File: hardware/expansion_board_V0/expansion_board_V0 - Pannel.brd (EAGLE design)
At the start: 212 x 132 mm, 499 parts, among them CON1 ELEC, CON10 M5, CON11 M2, CON12 M4, CON13 M1, CON14 ESC0, CON15 CON10_2_2.54, CON16 CON10_2_2.54, CON17 ESC1, CON18 UART0, CON19 QEI1, CON2 SERVO, CON20 AN0, CON21 S0, CON22 IO0, CON23 AN1, CON24 S1, CON25 IO1, CON26 UART1, CON27 QEI0, CON28 AN2, CON29 S2, CON3 LIPO_MOT, CON30 IO2, CON31 TELEM, CON32 QEI3, CON33 AN3, CON34 S3, CON35 IO3, CON36 BALISE, CON37 AN4, CON38 S4, CON39 IO4, CON4 LIPO_MOT, CON40 SPI0, CON41 QEI2, CON42 AN5, CON43 S5, CON44 IO5, CON45 SPI1, CON46 AN6, CON47 S6, CON48 IO6, CON49 I2C0, CON5 LIPO_MOT, CON50 AN7, CON51 S7, CON52 IO7, CON53 I2C1, CON54 USB2, CON55 USB3, CON56 USBfpga, CON57 FPGA_GPIO0, CON58 FPGA_GPIO1, CON59 FPGA_LTC, CON6 LIPO_MOT, CON60 USB3, CON61 CON5_2.54S, CON62 CON5_2.54S, CON63 CON5_2.54S, CON64 CON5_2.54S, CON7 FPGApower, CON8 M0, CON9 M3, IC1 ADS1258, IC2 ADS1278, IC3 REF5030I, IC4 REF5025I, J1 NC, J10 0, J11 0, J12 0, J13 0, J14 0, J15 0, J16 0, J17 0, J18 0, J19 0, J2 nc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

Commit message: -
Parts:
- added C200, C201, C202, C203, C204, C205, C206, C207, C208, C209, C210, C211: 2u, iocene:CAPC1608X95N
- added CON65, CON66, CON67, CON68, CON69, CON70, CON71, CON72, CON73, CON74, CON75, CON76: CON5_2.54S, iocene:CON254P1270X400-5S
- added R111, R112, R113, R114, R115, R116, R117, R118, R119, R120, R121, R122: 10k, iocene:RESC1005X40N
- added U41, U47, U53: VL53L0X, iocene:VL53L0X
- added U42, U44, U48, U50, U54, U56: TCA6408A, iocene:QFN50P300X300X80-17N
- added U43, U45, U49, U51, U55, U57: LP5900SD-2.8, iocene:SON65P250X220X80-7N
- added U46, U52, U58: VL6180X, iocene:VL6180X
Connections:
- new net GND1: C200.P$2, C201.P$2, C202.P$2, C203.P$2, CON65.1, CON66.1, CON67.1, CON68.1, R111.2, R112.2, R113.2, R114.2, U41.P$12, U41.P$2, U41.P$3, U41.P$4, U41.P$6, U42.GND, U42.P$16, U42.P$6, U43.2, U43.3, U43.5, U43.GND, U44.GND, U44.P$16, U44.P$6, U45.2, U45.3, U45.5, U45.GND, U46.P$11, U46.P$12, U46.P$2, U46.P$3, U46.P$7, U46.P$9
- new net GND2: C204.P$2, C205.P$2, C206.P$2, C207.P$2, CON69.1, CON70.1, CON71.1, CON72.1, R115.2, R116.2, R117.2, R118.2, U47.P$12, U47.P$2, U47.P$3, U47.P$4, U47.P$6, U48.GND, U48.P$16, U48.P$6, U49.2, U49.3, U49.5, U49.GND, U50.GND, U50.P$16, U50.P$6, U51.2, U51.3, U51.5, U51.GND, U52.P$11, U52.P$12, U52.P$2, U52.P$3, U52.P$7, U52.P$9
- new net GND3: C208.P$2, C209.P$2, C210.P$2, C211.P$2, CON73.1, CON74.1, CON75.1, CON76.1, R119.2, R120.2, R121.2, R122.2, U53.P$12, U53.P$2, U53.P$3, U53.P$4, U53.P$6, U54.GND, U54.P$16, U54.P$6, U55.2, U55.3, U55.5, U55.GND, U56.GND, U56.P$16, U56.P$6, U57.2, U57.3, U57.5, U57.GND, U58.P$11, U58.P$12, U58.P$2, U58.P$3, U58.P$7, U58.P$9
- new net N$107: CON66.3, R112.1, U42.P$1
- new net N$108: CON65.2, CON66.2, U41.P$9, U42.P$13
- new net N$109: CON65.4, CON66.4, U41.P$10, U42.P$12
- new net N$122: CON65.3, U42.P$10
- new net N$137: C201.P$1, CON65.5, CON66.5, U43.4, U43.6
- new net N$140: C200.P$1, U41.P$1, U41.P$11, U42.P$14, U42.P$15, U43.1
- new net N$141: C203.P$1, CON67.5, CON68.5, U45.4, U45.6
- new net N$142: CON67.4, CON68.4, U44.P$12, U46.P$5
- new net N$143: CON67.2, CON68.2, U44.P$13, U46.P$6
- new net N$144: C202.P$1, U44.P$14, U44.P$15, U45.1, U46.P$10, U46.P$8
- new net N$145: CON68.3, R114.1, U44.P$1
- new net N$146: CON67.3, U44.P$10
- new net N$147: R113.1, U44.P$4, U46.P$4
- new net N$148: R115.1, U47.P$5, U48.P$4
- new net N$152: CON70.3, R116.1, U48.P$1
- new net N$165: CON69.2, CON70.2, U47.P$9, U48.P$13
- new net N$179: CON69.4, CON70.4, U47.P$10, U48.P$12
- new net N$183: CON69.3, U48.P$10
- new net N$186: C205.P$1, CON69.5, CON70.5, U49.4, U49.6
- new net N$194: C204.P$1, U47.P$1, U47.P$11, U48.P$14, U48.P$15, U49.1
- new net N$197: C207.P$1, CON71.5, CON72.5, U51.4, U51.6
- new net N$203: CON71.4, CON72.4, U50.P$12, U52.P$5
- new net N$209: CON71.2, CON72.2, U50.P$13, U52.P$6
- new net N$215: C206.P$1, U50.P$14, U50.P$15, U51.1, U52.P$10, U52.P$8
- new net N$216: CON72.3, R118.1, U50.P$1
- new net N$217: CON71.3, U50.P$10
- new net N$218: R117.1, U50.P$4, U52.P$4
- new net N$222: R119.1, U53.P$5, U54.P$4
- new net N$226: CON74.3, R120.1, U54.P$1
- new net N$227: CON73.2, CON74.2, U53.P$9, U54.P$13
- new net N$228: CON73.4, CON74.4, U53.P$10, U54.P$12
- new net N$229: CON73.3, U54.P$10
- new net N$230: C209.P$1, CON73.5, CON74.5, U55.4, U55.6
- new net N$231: C208.P$1, U53.P$1, U53.P$11, U54.P$14, U54.P$15, U55.1
- new net N$233: C211.P$1, CON75.5, CON76.5, U57.4, U57.6
- new net N$234: CON75.4, CON76.4, U56.P$12, U58.P$5
- new net N$235: CON75.2, CON76.2, U56.P$13, U58.P$6
- new net N$236: C210.P$1, U56.P$14, U56.P$15, U57.1, U58.P$10, U58.P$8
- new net N$237: CON76.3, R122.1, U56.P$1
- new net N$238: CON75.3, U56.P$10
- new net N$239: R121.1, U56.P$4, U58.P$4
- new net N$98: R111.1, U41.P$5, U42.P$4
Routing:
- net GND3: track 0.00 -> 70.3 mm, vias 0 -> 63
- net GND2: track 0.00 -> 70.3 mm, vias 0 -> 63
- net GND1: track 0.00 -> 70.3 mm, vias 0 -> 63
- net N$234: track 0.00 -> 22.5 mm, vias 0 -> 1
- net N$203: track 0.00 -> 22.5 mm, vias 0 -> 1
- net N$142: track 0.00 -> 22.5 mm, vias 0 -> 1
- net N$230: track 0.00 -> 21.2 mm
- net N$186: track 0.00 -> 21.2 mm
- net N$137: track 0.00 -> 21.2 mm
- net N$233: track 0.00 -> 21.0 mm
- net N$197: track 0.00 -> 21.0 mm
- net N$141: track 0.00 -> 21.0 mm
- net N$228: track 0.00 -> 20.8 mm, vias 0 -> 1
- net N$179: track 0.00 -> 20.8 mm, vias 0 -> 1
- net N$109: track 0.00 -> 20.8 mm, vias 0 -> 1
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- added copper zone on layer 1, net GND1
- added copper zone on layer 15, net GND1
- added copper zone on layer 16, net GND1
- added copper zone on layer 2, net GND1
- added copper zone on layer 1, net GND2
- added copper zone on layer 15, net GND2
- added copper zone on layer 16, net GND2
- added copper zone on layer 2, net GND2
- added copper zone on layer 1, net GND3
- added copper zone on layer 15, net GND3
- added copper zone on layer 16, net GND3
- added copper zone on layer 2, net GND3
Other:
- outline, holes or cut-outs redrawn

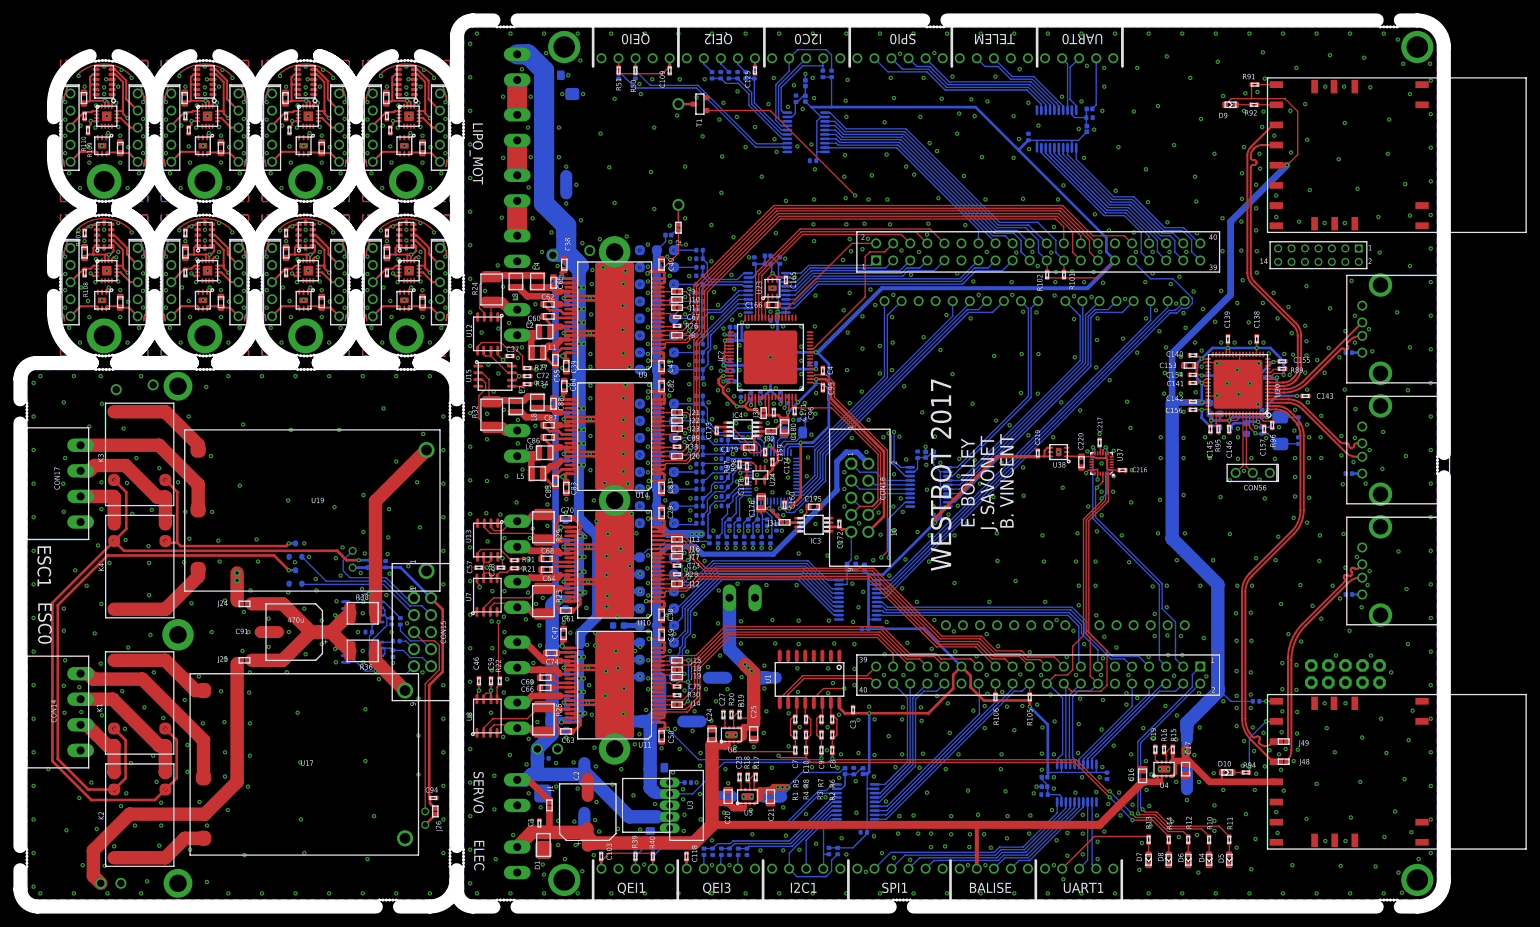
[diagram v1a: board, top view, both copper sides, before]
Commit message: PCB envoyé chez eurocircuit
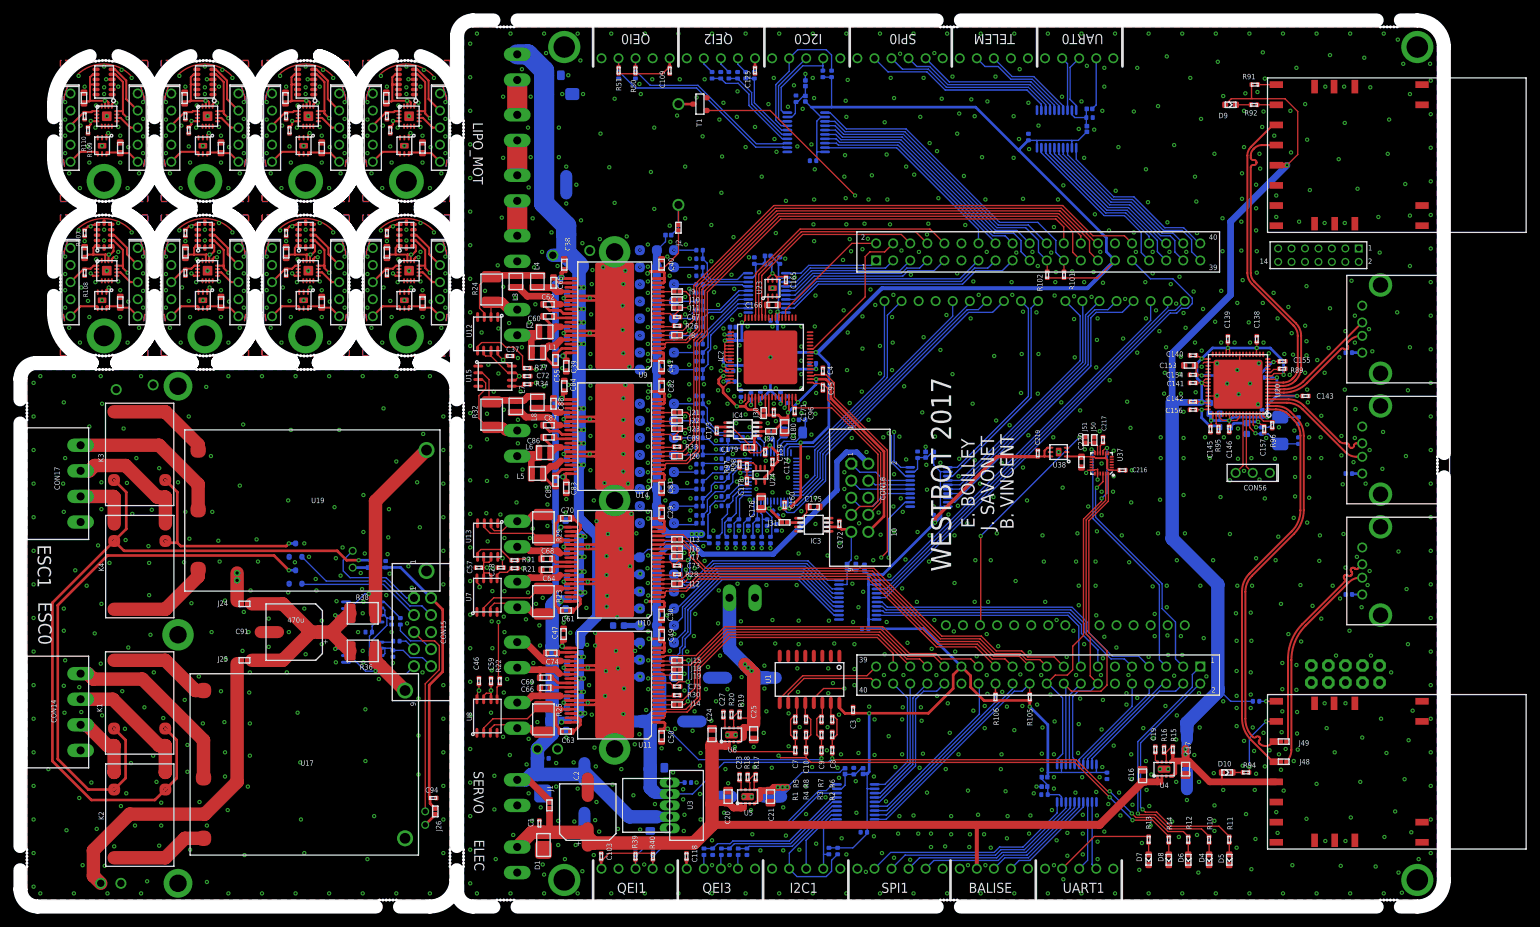
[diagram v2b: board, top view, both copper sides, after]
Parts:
- added J50, J51: (no value), iocene:JUMC1005X50N
- moved C217 0.64 mm to (-49.8, 3.50)
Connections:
- new net S$1: J51.P$2, U29.RESET
- net GND: now also J50.P$2
- net IMU_FSYNC: now also J50.P$1, J51.P$1
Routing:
- net S$1: track 0.00 -> 35.0 mm, vias 0 -> 2
- net IMU_FSYNC: track 0.00 -> 3.09 mm
- net REGOUT1: track 1.16 -> 1.69 mm
- net GND: vias 1564 -> 1566
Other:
- outline, holes or cut-outs redrawn

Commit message: Derniere modif elec
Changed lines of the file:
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@@
 <layer number="18" name="Vias" color="2" fill="1" visible="yes" active="yes"/>
 <layer number="19" name="Unrouted" color="6" fill="1" visible="no" active="yes"/>
-<layer number="20" name="Dimension" color="15" fill="1" visible="yes" active="yes"/>
+<layer number="20" name="Dimension" color="15" fill="1" visible="no" active="yes"/>
 <layer number="21" name="tPlace" color="7" fill="1" visible="no" active="yes"/>
 <layer number="22" name="bPlace" color="7" fill="1" visible="no" active="yes"/>
@@
 <layer number="39" name="tKeepout" color="4" fill="11" visible="no" active="yes"/>
 <layer number="40" name="bKeepout" color="1" fill="11" visible="no" active="yes"/>
-<layer number="41" name="tRestrict" color="4" fill="10" visible="no" active="yes"/>
-<layer number="42" name="bRestrict" color="1" fill="10" visible="no" active="yes"/>
+<layer number="41" name="tRestrict" color="4" fill="10" visible="yes" active="yes"/>
+<layer number="42" name="bRestrict" color="1" fill="10" visible="yes" active="yes"/>
 <layer number="43" name="vRestrict" color="2" fill="10" visible="no" active="yes"/>
 <layer number="44" name="Drills" color="7" fill="1" visible="no" active="yes"/>
 <layer number="45" name="Holes" color="7" fill="1" visible="no" active="yes"/>
 <layer number="46" name="Milling" color="3" fill="1" visible="no" active="yes"/>
-<layer number="47" name="Measures" color="7" fill="1" visible="yes" active="yes"/>
+<layer number="47" name="Measures" color="7" fill="1" visible="no" active="yes"/>
 <layer number="48" name="Document" color="5" fill="1" visible="no" active="yes"/>
-<layer number="49" name="Reference" color="7" fill="1" visible="yes" active="yes"/>
+<layer number="49" name="Reference" color="7" fill="1" visible="no" active="yes"/>
 <layer number="50" name="dxf" color="7" fill="1" visible="no" active="no"/>
 <layer number="51" name="tDocu" color="7" fill="1" visible="no" active="yes"/>
@@
 <vertex x="-195" y="15"/>
 </polygon>
+<hole x="-3.18" y="31.12" drill="3.2"/>
+<hole x="-3.18" y="-31.12" drill="3.2"/>
 </plain>
 <attributes>
@@
 <via x="-16.5" y="-39.4" extent="1-16" drill="0.3" diameter="0.65"/>
 <via x="-11.2" y="-40.8" extent="1-16" drill="0.3" diameter="0.65"/>
-<via x="-6.9" y="-31.1" extent="1-16" drill="0.3" diameter="0.65"/>
+<via x="-5.4" y="-33" extent="1-16" drill="0.3" diameter="0.65"/>
 <via x="-15.1" y="-28.6" extent="1-16" drill="0.3" diameter="0.65"/>
 <via x="-9.9" y="-28.6" extent="1-16" drill="0.3" diameter="0.65"/>
 <via x="-13.1" y="-24.9" extent="1-16" drill="0.3" diameter="0.65"/>
-<via x="-4.4" y="-26.9" extent="1-16" drill="0.3" diameter="0.65"/>
+<via x="-5.3" y="-28.7" extent="1-16" drill="0.3" diameter="0.65"/>
 <via x="-4.6" y="-18.7" extent="1-16" drill="0.3" diameter="0.65"/>
 <via x="-5.8" y="-13.1" extent="1-16" drill="0.3" diameter="0.65"/>
@@
 <via x="-16" y="23.1" extent="1-16" drill="0.3" diameter="0.65"/>
 <via x="-12.8" y="27.2" extent="1-16" drill="0.3" diameter="0.65"/>
-<via x="-8.6" y="31.4" extent="1-16" drill="0.3" diameter="0.65"/>
-<via x="-4.1" y="29.4" extent="1-16" drill="0.3" diameter="0.65"/>
+<via x="-5.4" y="32.8" extent="1-16" drill="0.3" diameter="0.65"/>
+<via x="-5.1" y="29" extent="1-16" drill="0.3" diameter="0.65"/>
 <via x="-8.8" y="36.7" extent="1-16" drill="0.3" diameter="0.65"/>
 <via x="-20.6" y="36" extent="1-16" drill="0.3" diameter="0.65"/>
@@
 <via x="-41.6" y="-10.4" extent="1-16" drill="0.3" diameter="0.65"/>
 <contactref element="J50" pad="P$2"/>
+<via x="-68.9" y="-20.6" extent="1-16" drill="0.3" diameter="0.65"/>
+<via x="-68.8" y="-14.4" extent="1-16" drill="0.3" diameter="0.65"/>
 <wire x1="-204.55" y1="22.2" x2="-204.55" y2="22.2" width="0" layer="19" extent="1-2"/>
 <wire x1="-204.55" y1="22.2" x2="-204.55" y2="22.2" width="0" layer="19" extent="2-15"/>
@@
 <wire x1="-192.6" y1="44.25" x2="-192.6" y2="44.25" width="0" layer="19" extent="2-15"/>
 <wire x1="-192.6" y1="44.25" x2="-192.6" y2="44.25" width="0" layer="19" extent="1-2"/>
-<via x="-68.9" y="-20.6" extent="1-16" drill="0.3" diameter="0.65"/>
-<via x="-68.8" y="-14.4" extent="1-16" drill="0.3" diameter="0.65"/>
 </signal>
 <signal name="3V3">
